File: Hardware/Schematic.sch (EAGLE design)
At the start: 103 parts, among them IC1 BD5229G-TR, IC4 XC6220A331MR-G, J1 FH34SRJ-24S-0.5SH_99_, J2 SAMACSYS_PARTS_USB4110-GF-A, J3 QWIIC_RIGHT_ANGLE, J4 112A-TAAR-R03_ATTEND, Q1 20V/4.2A/52mΩ/1.4W, Q2 20V/4.2A/52mΩ/1.4W, Q3 SI1308EDL-T1-GE3, U1 W25Q512JVEIQ, U2 ESP32-C6-WROOM-1-N8, U3 DS3231SN#, U4 MAX17048G+T10

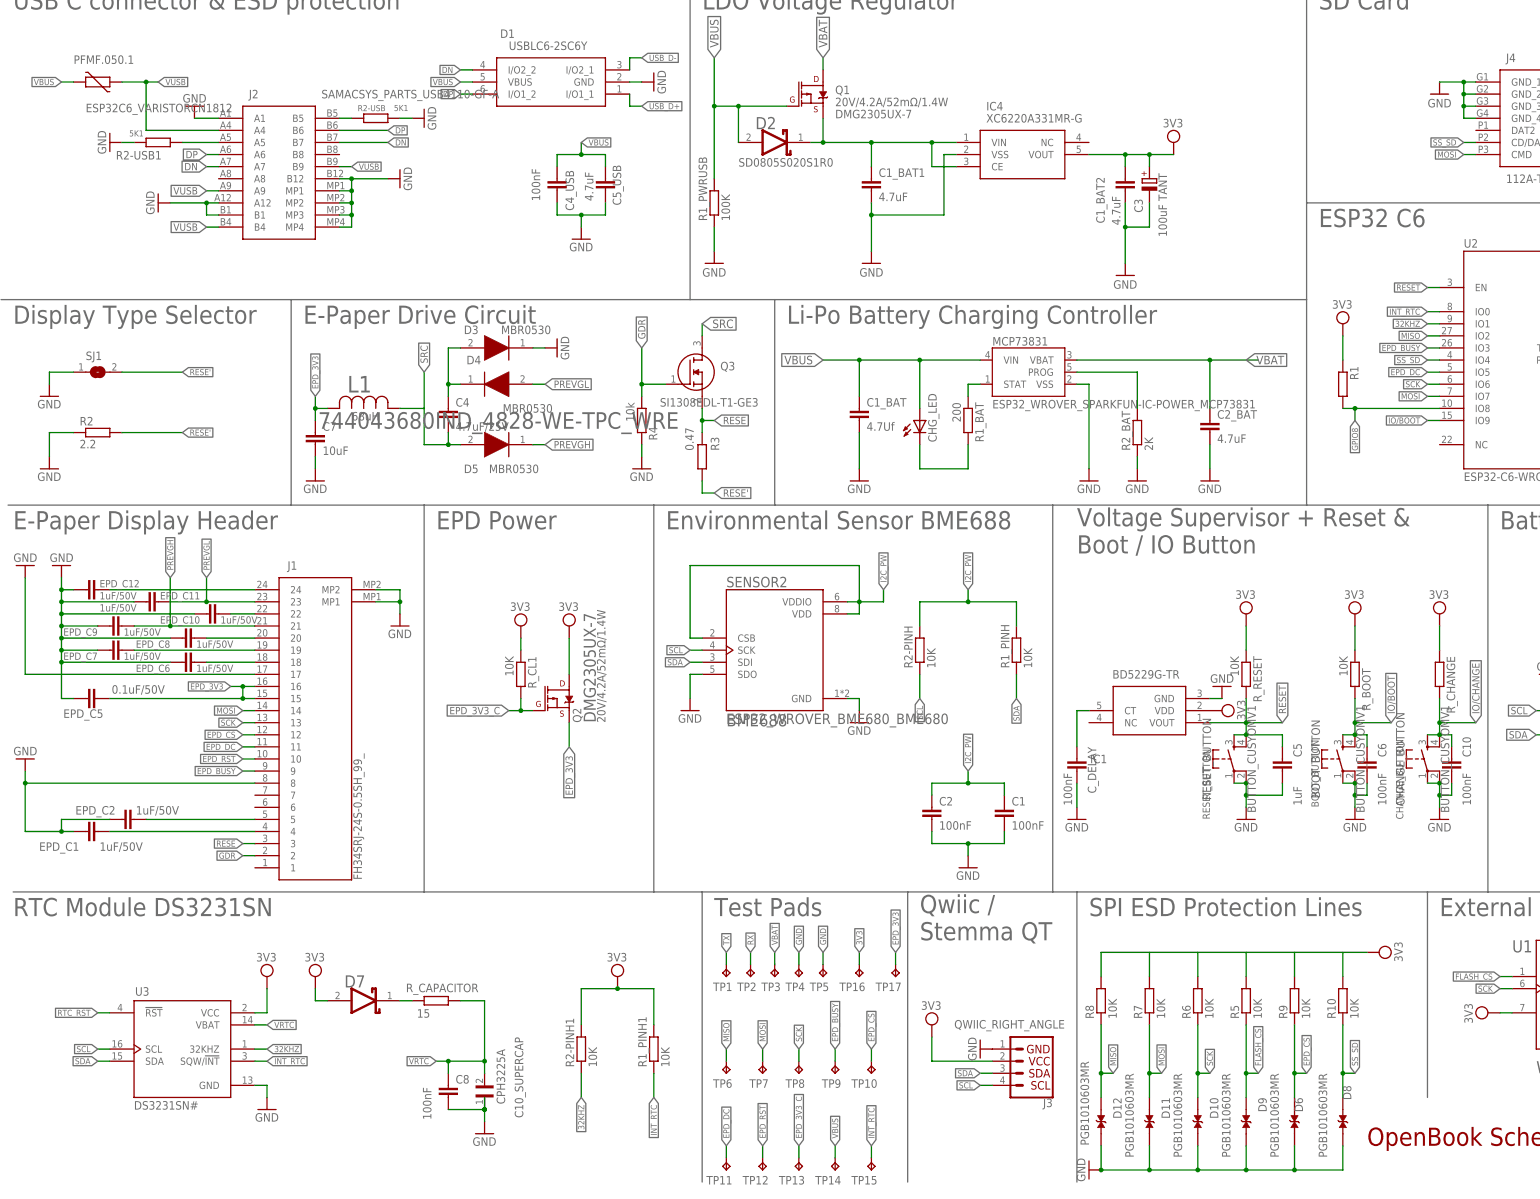
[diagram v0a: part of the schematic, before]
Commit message: Remaining exploded view and manufacturing
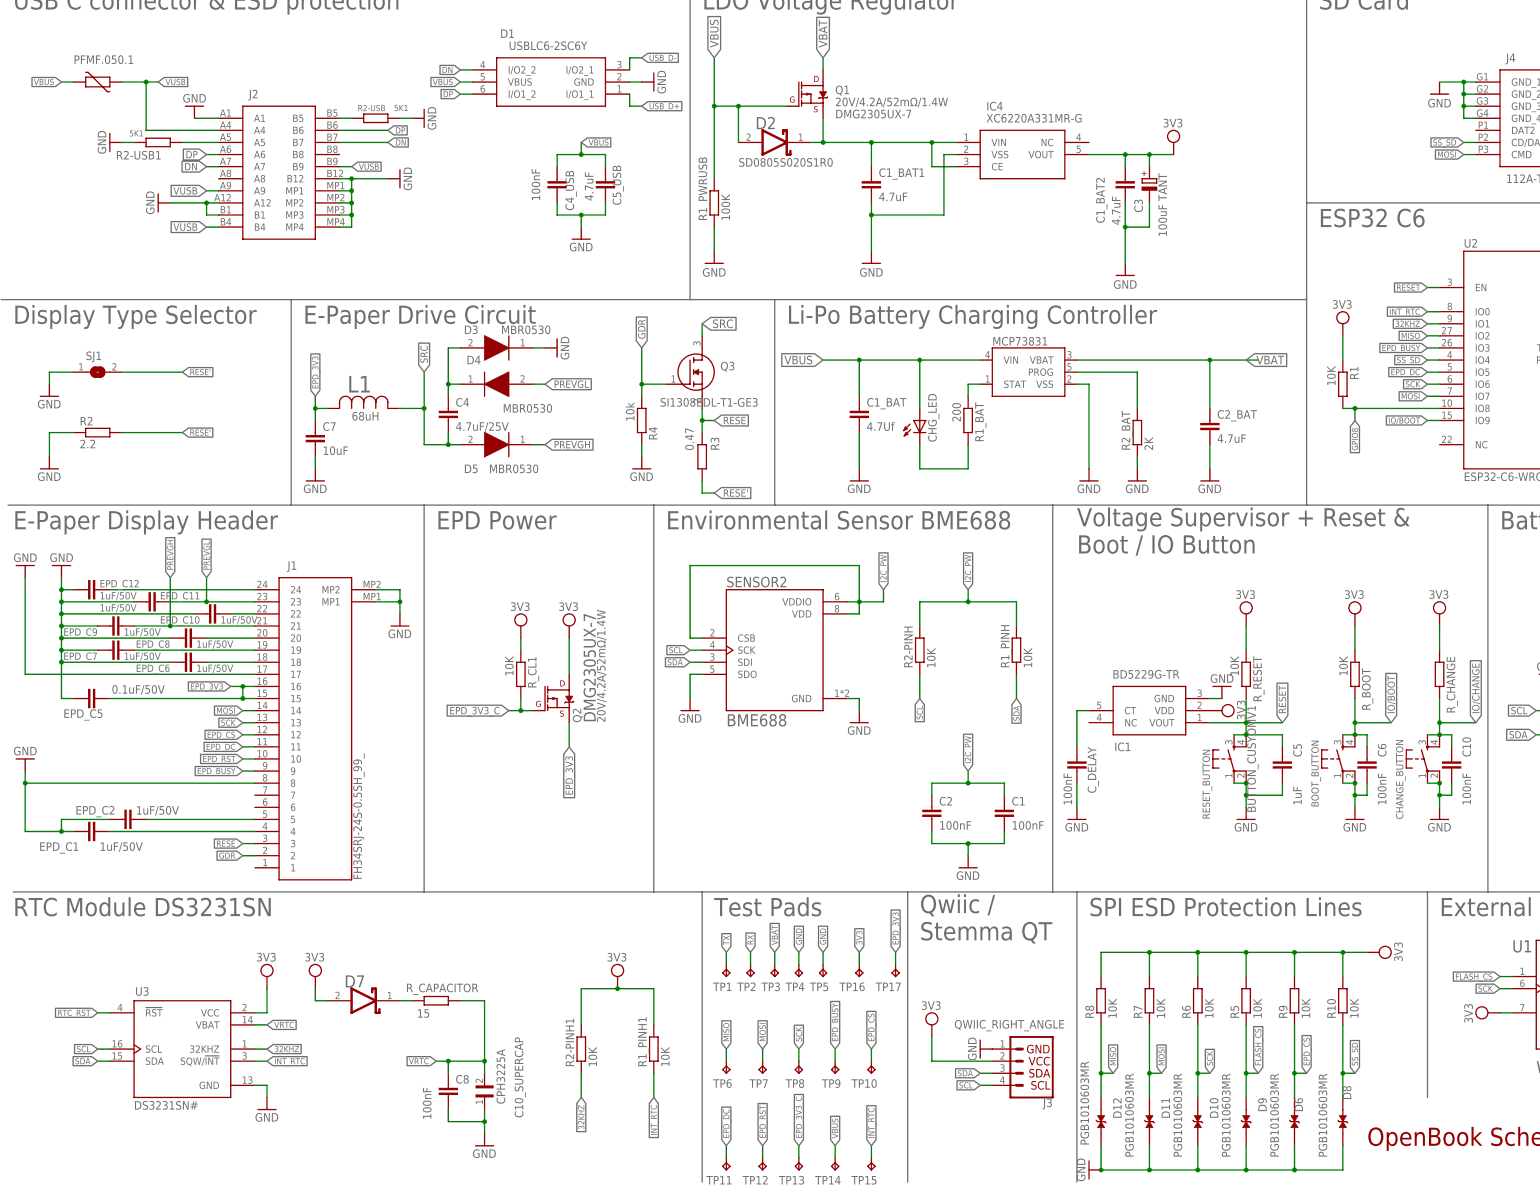
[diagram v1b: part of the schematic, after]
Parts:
- R1: value (none) -> 10K
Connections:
- removed net N$26: R7.2
- removed net N$27: R6.2
- removed net N$28: R5.2
- removed net N$29: R9.2
- removed net N$30: R10.2
- net 3V3: now also R10.2, R5.2, R6.2, R7.2, R9.2

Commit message: FInal version of files. Remaining gerbers
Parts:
- R_CHANGE: value (none) -> 10K
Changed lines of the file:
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@@
 </classes>
 <parts>
-<part name="FRAME1" library="Frames" library_urn="urn:adsk.eagle:library:42976481" deviceset="A3L-LOC" device=""/>
+<part name="FRAME1" library="Frames" library_urn="urn:adsk.eagle:library:42976481" deviceset="A3L-LOC" device="" value="OpenBook"/>
 <part uuid="2882400016" name="J2" library="DeskAssistant v19 v1" library_urn="urn:adsk.wipprod:fs.file:vf.i3aUetO7RU6W5A7ASBjTVA" deviceset="SAMACSYS_PARTS_USB4110-GF-A" device="" package3d_urn="urn:adsk.eagle:package:47601148/1" override_locally_modified="yes"/>
 <part name="GND1" library="DeskAssistant v19 v1" library_urn="urn:adsk.wipprod:fs.file:vf.i3aUetO7RU6W5A7ASBjTVA" deviceset="GND" device=""/>
@@
 <part name="C6" library="DeskAssistant v19 v1" library_urn="urn:adsk.wipprod:fs.file:vf.i3aUetO7RU6W5A7ASBjTVA" deviceset="EAGLE-LTSPICE_C" device="C0402" value="100nF"/>
 <part name="BOOT_BUTTON" library="DeskAssistant v19 v1" library_urn="urn:adsk.wipprod:fs.file:vf.i3aUetO7RU6W5A7ASBjTVA" deviceset="BUTTON_CUSYOMV1" device=""/>
-<part name="R_CHANGE" library="DeskAssistant v19 v1" library_urn="urn:adsk.wipprod:fs.file:vf.i3aUetO7RU6W5A7ASBjTVA" deviceset="ESP32_WROVER_EAGLE-LTSPICE_R" device="R0402" package3d_urn="urn:adsk.eagle:package:47601124/1"/>
+<part name="R_CHANGE" library="DeskAssistant v19 v1" library_urn="urn:adsk.wipprod:fs.file:vf.i3aUetO7RU6W5A7ASBjTVA" deviceset="ESP32_WROVER_EAGLE-LTSPICE_R" device="R0402" package3d_urn="urn:adsk.eagle:package:47601124/1" value="10K"/>
 <part name="SUPPLY10" library="DeskAssistant v19 v1" library_urn="urn:adsk.wipprod:fs.file:vf.i3aUetO7RU6W5A7ASBjTVA" deviceset="3V3-CIRCLE" device="" value="3V3"/>
 <part name="SUPPLY11" library="DeskAssistant v19 v1" library_urn="urn:adsk.wipprod:fs.file:vf.i3aUetO7RU6W5A7ASBjTVA" deviceset="3V3-CIRCLE" device="" value="3V3"/>
@@
 <instance part="BOOT_BUTTON" gate="G$1" x="160.02" y="121.92" smashed="yes" rot="R90"/>
 <instance part="R_CHANGE" gate="G$1" x="180.34" y="139.7" smashed="yes" rot="R270">
-<attribute name="VALUE" x="177.038" y="143.51" size="1.778" layer="96" rot="R270"/>
 <attribute name="NAME" x="181.8386" y="143.51" size="1.778" layer="95" rot="R270"/>
-<attribute name="VALUE" x="177.038" y="143.51" size="1.778" layer="96" rot="R270"/>
+<attribute name="VALUE" x="177.038" y="146.05" size="1.778" layer="96" rot="R270"/>
 </instance>
 <instance part="SUPPLY10" gate="G$1" x="162.56" y="152.4" smashed="yes">
@@
 <attribute name="VALUE" x="151.384" y="112.141" size="1.778" layer="96" rot="R90"/>
 </instance>
-<instance part="RESET_BUTTON" gate="G$1" x="137.16" y="121.92" smashed="yes" rot="R90">
-<attribute name="VALUE" x="139.954" y="121.92" size="1.778" layer="96" font="vector" rot="R90" align="top-center"/>
-</instance>
+<instance part="RESET_BUTTON" gate="G$1" x="137.16" y="121.92" smashed="yes" rot="R90"/>
 <instance part="SUPPLY12" gate="G$1" x="139.7" y="152.4" smashed="yes">
 <attribute name="VALUE" x="139.573" y="155.575" size="1.778" layer="96" align="bottom-center"/>
